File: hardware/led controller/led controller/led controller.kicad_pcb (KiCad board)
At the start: 2 copper layers, 48.3 x 55.9 mm, 4 parts, among them J1 Conn_01x03, J2 Conn_01x03, J3 Conn_01x02

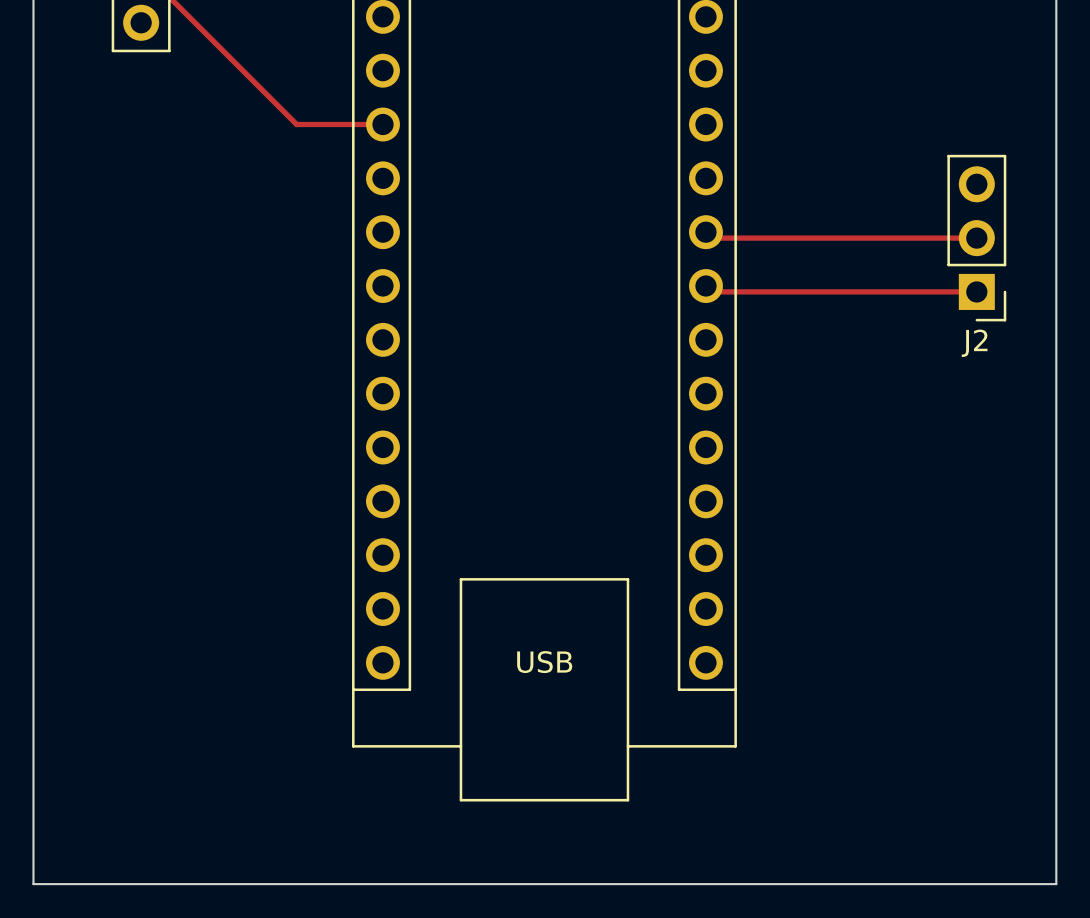
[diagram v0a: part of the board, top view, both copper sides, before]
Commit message: defined commands
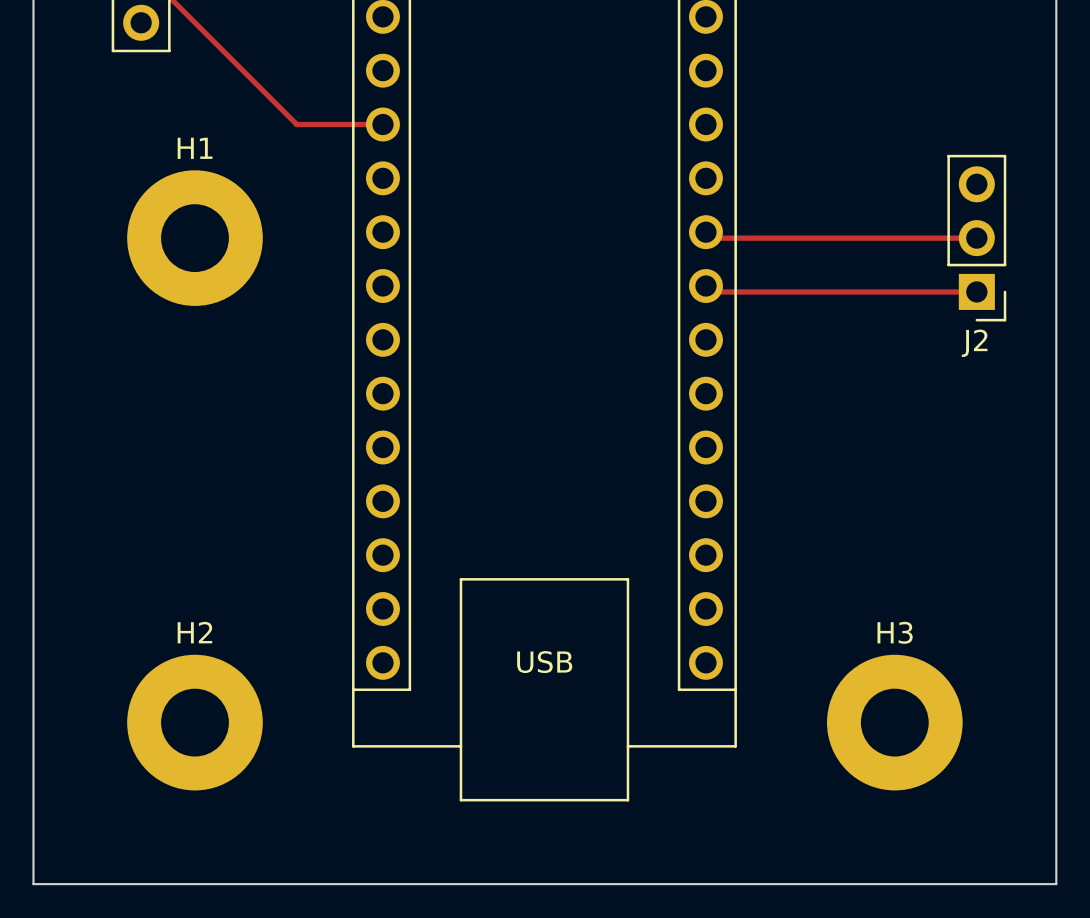
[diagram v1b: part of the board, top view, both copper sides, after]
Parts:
- added H1: MountingHole_3.2mm_M3_Pad, MountingHole:MountingHole_3.2mm_M3_Pad, F.Cu at (132.1, 88.9)
- added H2: MountingHole_3.2mm_M3_Pad, MountingHole:MountingHole_3.2mm_M3_Pad, F.Cu at (132.1, 111.8)
- added H3: MountingHole_3.2mm_M3_Pad, MountingHole:MountingHole_3.2mm_M3_Pad, F.Cu at (165.1, 111.8)
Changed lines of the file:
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@@
     )
+  )
+  (footprint "MountingHole:MountingHole_3.2mm_M3_Pad" (layer "F.Cu")
+    (at 165.1 111.76)
+    (descr "Mounting Hole 3.2mm, M3")
+    (tags "mounting hole 3.2mm m3")
+    (attr exclude_from_pos_files exclude_from_bom)
+    (fp_text reference "H3" (at 0 -4.2) (layer "F.SilkS")
+      (effects (font (size 1 1) (thickness 0.15)))
+    )
+    (fp_text value "MountingHole_3.2mm_M3_Pad" (at 0 4.2) (layer "F.Fab")
+      (effects (font (size 1 1) (thickness 0.15)))
+    )
+    (fp_text user "${REFERENCE}" (at 0 0) (layer "F.Fab")
+      (effects (font (size 1 1) (thickness 0.15)))
+    )
+    (fp_circle (center 0 0) (end 3.2 0) (layer "Cmts.User") (width 0.15) (fill none))
+    (fp_circle (center 0 0) (end 3.45 0) (layer "F.CrtYd") (width 0.05) (fill none))
+    (pad "1" thru_hole circle (at 0 0) (size 6.4 6.4) (drill 3.2) (layers *.Cu *.Mask))
   )
   (footprint "Connector_PinHeader_2.54mm:PinHeader_1x03_P2.54mm_Vertical" (layer "F.Cu")
@@
     )
   )
+  (footprint "MountingHole:MountingHole_3.2mm_M3_Pad" (layer "F.Cu")
+    (at 132.08 111.76)
+    (descr "Mounting Hole 3.2mm, M3")
+    (tags "mounting hole 3.2mm m3")
+    (attr exclude_from_pos_files exclude_from_bom)
+    (fp_text reference "H2" (at 0 -4.2) (layer "F.SilkS")
+      (effects (font (size 1 1) (thickness 0.15)))
+    )
+    (fp_text value "MountingHole_3.2mm_M3_Pad" (at 0 4.2) (layer "F.Fab")
+      (effects (font (size 1 1) (thickness 0.15)))
+    )
+    (fp_text user "${REFERENCE}" (at 0 0) (layer "F.Fab")
+      (effects (font (size 1 1) (thickness 0.15)))
+    )
+    (fp_circle (center 0 0) (end 3.2 0) (layer "Cmts.User") (width 0.15) (fill none))
+    (fp_circle (center 0 0) (end 3.45 0) (layer "F.CrtYd") (width 0.05) (fill none))
+    (pad "1" thru_hole circle (at 0 0) (size 6.4 6.4) (drill 3.2) (layers *.Cu *.Mask))
+  )
+  (footprint "MountingHole:MountingHole_3.2mm_M3_Pad" (layer "F.Cu")
+    (at 132.08 88.9)
+    (descr "Mounting Hole 3.2mm, M3")
+    (tags "mounting hole 3.2mm m3")
+    (attr exclude_from_pos_files exclude_from_bom)
+    (fp_text reference "H1" (at 0 -4.2) (layer "F.SilkS")
+      (effects (font (size 1 1) (thickness 0.15)))
+    )
+    (fp_text value "MountingHole_3.2mm_M3_Pad" (at 0 4.2) (layer "F.Fab")
+      (effects (font (size 1 1) (thickness 0.15)))
+    )
+    (fp_text user "${REFERENCE}" (at 0 0) (layer "F.Fab")
+      (effects (font (size 1 1) (thickness 0.15)))
+    )
+    (fp_circle (center 0 0) (end 3.2 0) (layer "Cmts.User") (width 0.15) (fill none))
+    (fp_circle (center 0 0) (end 3.45 0) (layer "F.CrtYd") (width 0.05) (fill none))
+    (pad "1" thru_hole circle (at 0 0) (size 6.4 6.4) (drill 3.2) (layers *.Cu *.Mask))
+  )
   (gr_line (start 172.72 119.38) (end 124.46 119.38) (layer "Edge.Cuts") (width 0.1))

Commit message: Update PCB
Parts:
- added H4: MountingHole_3.2mm_M3_Pad, MountingHole:MountingHole_3.2mm_M3_Pad, F.Cu at (168.5, 67.8)
- added J4: Conn_01x15_Male, Connector_PinHeader_2.54mm:PinHeader_1x15_P2.54mm_Vertical, F.Cu at (136.7, 73.4)
- added J5: Conn_01x15_Male, Connector_PinHeader_2.54mm:PinHeader_1x15_P2.54mm_Vertical, F.Cu at (160.9, 73.4)
- J3: footprint Connector_PinHeader_2.54mm:PinHeader_1x02_P2.54mm_Vertical -> TerminalBlock:TerminalBlock_bornier-2_P5.08mm
- moved H1 20.7 mm to (129.4, 68.3)
- moved J1 7.26 mm to (129.9, 80.9)
- moved J3 7.12 mm to (168.4, 80.7), turned to 90 degrees
- moved H3 4.19 mm to (169.3, 111.6)
- moved H2 2.84 mm to (129.3, 111.3)
- moved J2 2.35 mm to (166.6, 91.4)
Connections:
- A1 pad 1: unconnected-(A1-Pad1) -> /D1
- A1 pad 10: unconnected-(A1-Pad10) -> /D7
- A1 pad 11: unconnected-(A1-Pad11) -> /D8
- A1 pad 12: unconnected-(A1-Pad12) -> /D9
- A1 pad 13: unconnected-(A1-Pad13) -> /D10
- A1 pad 14: unconnected-(A1-Pad14) -> /D11
- A1 pad 15: unconnected-(A1-Pad15) -> /D12
- A1 pad 16: unconnected-(A1-Pad16) -> /D13
- A1 pad 17: unconnected-(A1-Pad17) -> +3.3V
- A1 pad 18: unconnected-(A1-Pad18) -> /AREF
- A1 pad 19: unconnected-(A1-Pad19) -> /A0
- A1 pad 2: unconnected-(A1-Pad2) -> /D0
- A1 pad 20: unconnected-(A1-Pad20) -> /A1
- A1 pad 21: unconnected-(A1-Pad21) -> /A2
- A1 pad 22: unconnected-(A1-Pad22) -> /A3
- A1 pad 25: unconnected-(A1-Pad25) -> /A6
- A1 pad 26: unconnected-(A1-Pad26) -> /A7
- A1 pad 27: unconnected-(A1-Pad27) -> VCC
- A1 pad 28: unconnected-(A1-Pad28) -> /RST
- A1 pad 3: unconnected-(A1-Pad3) -> /RST
- A1 pad 6: unconnected-(A1-Pad6) -> /D3
- A1 pad 7: unconnected-(A1-Pad7) -> /D4
- A1 pad 8: unconnected-(A1-Pad8) -> /D5
- A1 pad 9: unconnected-(A1-Pad9) -> /D6
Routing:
- net /RST: track 0.00 -> 9.04 mm
- net +5V: track 41.7 -> 50.7 mm
- net VCC: track 0.00 -> 4.73 mm
- net /D13: track 0.00 -> 4.73 mm
- net /AREF: track 0.00 -> 4.73 mm
- net /A6: track 0.00 -> 4.73 mm
- net /A2: track 0.00 -> 4.73 mm
- net /A1: track 0.00 -> 4.73 mm
- net /A0: track 0.00 -> 4.73 mm
- net GND: track 0.00 -> 4.73 mm
- net /A7: track 0.00 -> 4.73 mm
- net /A3: track 0.00 -> 4.73 mm
- net +3.3V: track 0.00 -> 4.73 mm
- net /D1: track 0.00 -> 4.31 mm
- net /D9: track 0.00 -> 4.31 mm
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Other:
- board size 48.3 x 55.9 mm -> 49.9 x 52.8 mm
- board text added: "3V3"
- board text added: "5690 SubZero LED Controller 2023 V1"
- board text added: "5V"
- board text added: "5V IN"
- board text added: "A0"
- board text added: "A1"
- board text added: "A2"
- board text added: "A3"
- board text added: "A4"
- board text added: "A5"
- board text added: "A6"
- board text added: "A7"
- board text added: "AREF"
- board text added: "D10"
- board text added: "D11"
- board text added: "D12"
- board text added: "D13"
- board text added: "D2"
- board text added: "D3"
- board text added: "D4"
- board text added: "D5"
- board text added: "D6"
- board text added: "D7"
- board text added: "D8"
- board text added: "D9"
- board text added: "DOUT"
- board text added: "GND"
- board text added: "RST"
- board text added: "RX"
- board text added: "RoboRIO"
- board text added: "SCL"
- board text added: "SDA"
- board text added: "TX"
- board text added: "VIN"

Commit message: Update PCB
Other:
- board text added: "Arduino Nano R3"
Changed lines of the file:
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@@
       (drillshape 0)
       (scaleselection 1)
-      (outputdirectory "")
+      (outputdirectory "../")
     )
   )
@@
   (gr_line (start 124.333 116.332) (end 124.46 63.5) (layer "Edge.Cuts") (width 0.1))
   (gr_line (start 174.244 63.5) (end 174.244 116.332) (layer "Edge.Cuts") (width 0.1))
+  (gr_text "Arduino Nano R3" (at 148.336 91.186) (layer "B.SilkS")
+    (effects (font (size 1 1) (thickness 0.15)) (justify mirror))
+  )
   (gr_text "GND" (at 169.037 86.233 90) (layer "F.SilkS")
     (effects (font (size 0.762 0.762) (thickness 0.127)))
@@
     (effects (font (size 0.762 0.762) (thickness 0.127)))
   )
+  (dimension (type aligned) (layer "Dwgs.User")
+    (pts (xy 174.244 63.5) (xy 124.46 63.5))
+    (height 11.683999)
+    (gr_text "49.7840 mm" (at 149.352 50.666001) (layer "Dwgs.User")
+      (effects (font (size 1 1) (thickness 0.15)))
+    )
+    (format (units 3) (units_format 1) (precision 4))
+    (style (thickness 0.15) (arrow_length 1.27) (text_position_mode 0) (extension_height 0.58642) (extension_offset 0.5) keep_text_aligned)
+  )
+  (dimension (type aligned) (layer "Dwgs.User")
+    (pts (xy 124.46 63.5) (xy 124.333 116.332))
+    (height 14.126572)
+    (gr_text "52.8322 mm" (at 109.119972 89.879278 89.86227003) (layer "Dwgs.User")
+      (effects (font (size 1 1) (thickness 0.15)))
+    )
+    (format (units 3) (units_format 1) (precision 4))
+    (style (thickness 0.15) (arrow_length 1.27) (text_position_mode 0) (extension_height 0.58642) (extension_offset 0.5) keep_text_aligned)
+  )
   (segment (start 140.919 73.411) (end 140.95 73.38) (width 0.25) (layer "F.Cu") (net 1))

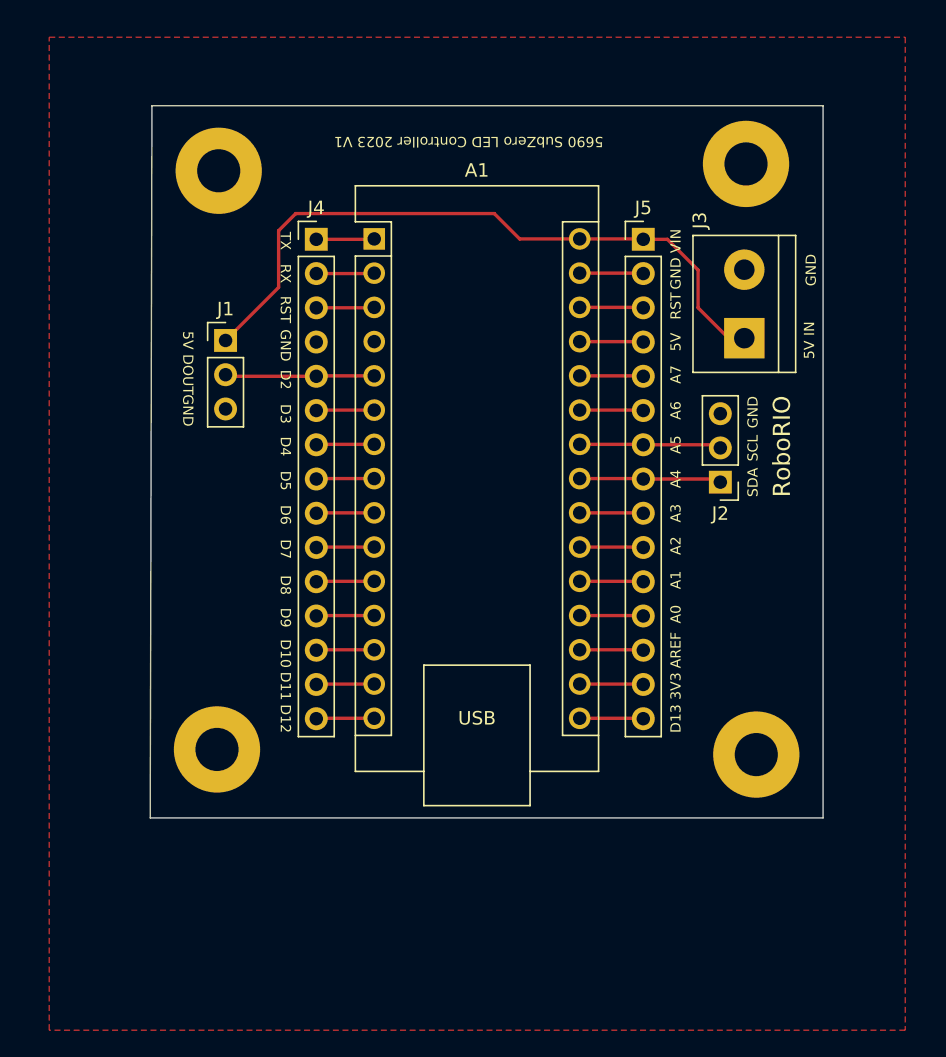
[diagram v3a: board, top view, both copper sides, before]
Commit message: Add ground plane to layer 2
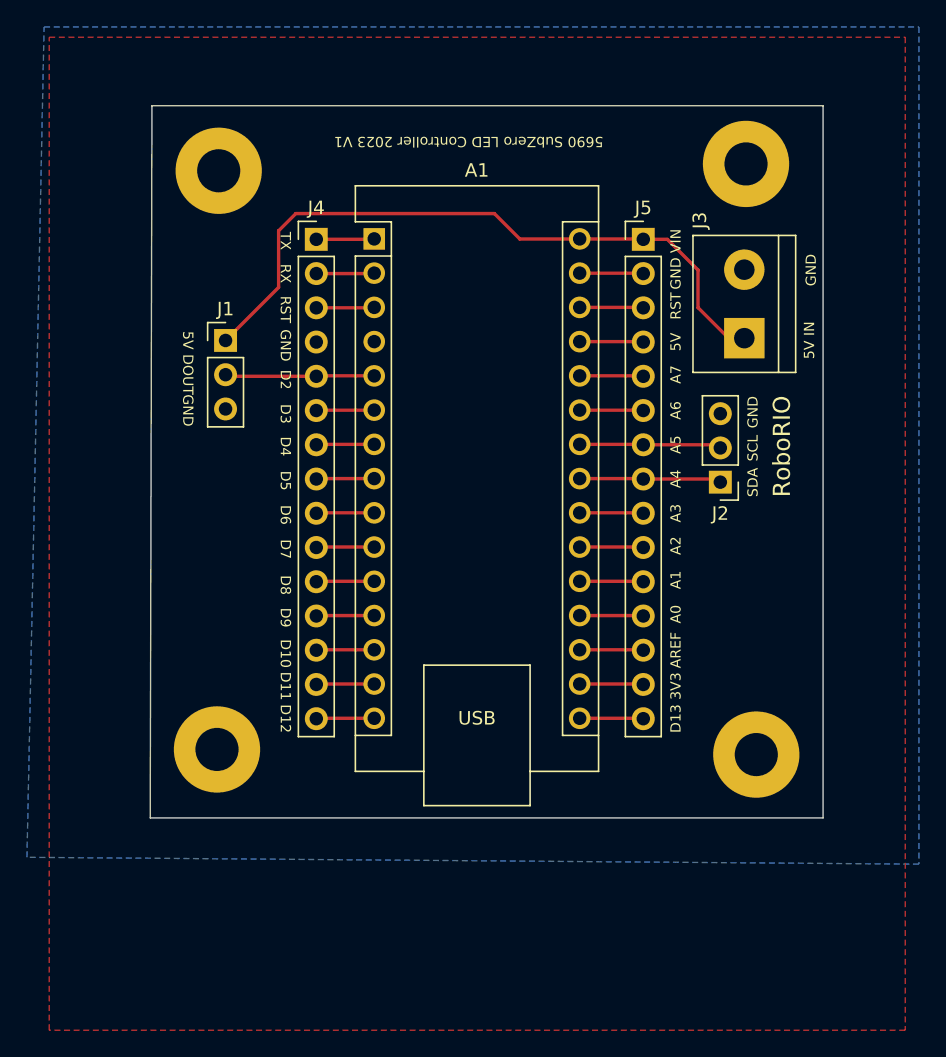
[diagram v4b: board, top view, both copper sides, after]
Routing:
- added copper zone on B.Cu, net GND
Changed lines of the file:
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@@
+    )
+  )
+  (zone (net 4) (net_name "GND") (layer "B.Cu") (hatch edge 0.508)
+    (connect_pads (clearance 0.508))
+    (min_thickness 0.254) (filled_areas_thickness no)
+    (fill yes (thermal_gap 0.508) (thermal_bridge_width 0.508))
+    (polygon
+      (pts
+        (xy 181.356 119.761)
+        (xy 115.189 119.253)
+        (xy 116.459 57.658)
+        (xy 181.356 57.658)
+      )
     )
   )
